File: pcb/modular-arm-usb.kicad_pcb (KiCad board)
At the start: 2 copper layers, 0 parts

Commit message: made a usb-a plug from usb-if and wikipedia docs
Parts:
- added CON1: ARM-SWD-HEADER, pin_array_5x2_50mil_smd, F.Cu at (142.5, 93.0)
- added P1: USB, USB_A_PCB, F.Cu at (115.6, 97.8)
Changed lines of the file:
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@@
 (kicad_pcb (version 3) (host pcbnew "(2013-07-07 BZR 4022)-stable")
   (general
-    (links 0)
-    (no_connects 0)
+    (links 3)
+    (no_connects 3)
     (area 0 0 0 0)
     (thickness 1.6)
@@
     (tracks 0)
     (zones 0)
-    (modules 0)
-    (nets 1)
+    (modules 2)
+    (nets 10)
   )
   (page A3)
@@
     (mod_text_size 1 1)
     (mod_text_width 0.15)
-    (pad_size 1.5 1.5)
-    (pad_drill 0.6)
+    (pad_size 1.143 7.6)
+    (pad_drill 0)
     (pad_to_mask_clearance 0)
     (aux_axis_origin 0 0)
-    (visible_elements FFFFFFBF)
+    (visible_elements 7FFFFFFF)
     (pcbplotparams
       (layerselection 3178497)
@@
   )
   (net 0 "")
+  (net 1 /lpc-mcu/SWCLK)
+  (net 2 /lpc-mcu/SWDIO)
+  (net 3 /lpc-mcu/SWO)
+  (net 4 /lpc-mcu/nRESET)
+  (net 5 /usb/DM)
+  (net 6 /usb/DP)
+  (net 7 GND)
+  (net 8 N-0000011)
+  (net 9 VUSB)
   (net_class Default "This is the default net class."
     (clearance 0.254)
@@
     (uvia_drill 0.127)
     (add_net "")
+    (add_net /lpc-mcu/SWCLK)
+    (add_net /lpc-mcu/SWDIO)
+    (add_net /lpc-mcu/SWO)
+    (add_net /lpc-mcu/nRESET)
+    (add_net /usb/DM)
+    (add_net /usb/DP)
+    (add_net GND)
+    (add_net N-0000011)
+    (add_net VUSB)
+  )
+  (module pin_array_5x2_50mil_smd (layer F.Cu)
+    (at 142.494 92.964)
+    (descr "Double rangee de contacts 2 x 4 pins")
+    (tags CONN)
+    (fp_text reference CON1 (at -4.445 0 90) (layer F.SilkS)
+      (effects (font (size 1.016 1.016) (thickness 0.2032)))
+    )
+    (fp_text value ARM-SWD-HEADER (at 4.318 0 90) (layer F.SilkS) hide
+      (effects (font (size 1.016 1.016) (thickness 0.2032)))
+    )
+    (fp_line (start -1.905 0.381) (end -3.302 0.381) (layer F.SilkS) (width 0.15))
+    (fp_line (start -3.302 0.381) (end -3.302 3.556) (layer F.SilkS) (width 0.15))
+    (fp_line (start -3.302 3.556) (end -1.905 3.556) (layer F.SilkS) (width 0.15))
+    (fp_line (start -2.54 1.524) (end -2.794 1.905) (layer F.SilkS) (width 0.15))
+    (fp_line (start -2.794 1.905) (end -2.413 1.905) (layer F.SilkS) (width 0.15))
+    (fp_line (start -2.413 1.905) (end -2.286 1.905) (layer F.SilkS) (width 0.15))
+    (fp_line (start -2.286 1.905) (end -2.54 1.524) (layer F.SilkS) (width 0.15))
+    (pad 10 smd rect (at 2.54 -1.95) (size 0.76 2.4)
+      (layers F.Cu F.Paste F.Mask)
+      (net 4 /lpc-mcu/nRESET)
+    )
+    (pad 9 smd rect (at 2.54 1.95) (size 0.76 2.4)
+      (layers F.Cu F.Paste F.Mask)
+      (net 7 GND)
+    )
+    (pad 8 smd rect (at 1.27 -1.95) (size 0.76 2.4)
+      (layers F.Cu F.Paste F.Mask)
+    )
+    (pad 7 smd rect (at 1.27 1.95) (size 0.76 2.4)
+      (layers F.Cu F.Paste F.Mask)
+    )
+    (pad 1 smd rect (at -2.54 1.95) (size 0.76 2.4)
+      (layers F.Cu F.Paste F.Mask)
+      (net 8 N-0000011)
+    )
+    (pad 2 smd rect (at -2.54 -1.95) (size 0.76 2.4)
+      (layers F.Cu F.Paste F.Mask)
+      (net 2 /lpc-mcu/SWDIO)
+    )
+    (pad 3 smd rect (at -1.27 1.95) (size 0.76 2.4)
+      (layers F.Cu F.Paste F.Mask)
+      (net 7 GND)
+    )
+    (pad 4 smd rect (at -1.27 -1.95) (size 0.76 2.4)
+      (layers F.Cu F.Paste F.Mask)
+      (net 1 /lpc-mcu/SWCLK)
+    )
+    (pad 5 smd rect (at 0 1.95) (size 0.76 2.4)
+      (layers F.Cu F.Paste F.Mask)
+      (net 7 GND)
+    )
+    (pad 6 smd rect (at 0 -1.95) (size 0.76 2.4)
+      (layers F.Cu F.Paste F.Mask)
+      (net 3 /lpc-mcu/SWO)
+    )
+    (model pin_array/pins_array_3x2.wrl
+      (at (xyz 0 0 0))
+      (scale (xyz 1 1 1))
+      (rotate (xyz 0 0 0))
+    )
+  )
+  (module USB_A_PCB (layer F.Cu)
+    (at 115.57 97.79 270)
+    (fp_text reference P1 (at 0.05 0.75 270) (layer F.SilkS) hide
+      (effects (font (size 1 1) (thickness 0.15)))
+    )
+    (fp_text value USB (at 0.125 -1.1 270) (layer F.SilkS)
+      (effects (font (size 1 1) (thickness 0.15)))
+    )
+    (fp_line (start -6 -8.65) (end -6 -1) (layer F.SilkS) (width 0.15))
+    (fp_line (start 6 -1) (end 6 -8.65) (layer F.SilkS) (width 0.15))
+    (fp_line (start -5 0) (end 5 0) (layer F.SilkS) (width 0.15))
+    (fp_arc (start 5 -1) (end 6 -1) (angle 90) (layer F.SilkS) (width 0.15))
+    (fp_arc (start -5 -1) (end -5 0) (angle 90) (layer F.SilkS) (width 0.15))
+    (fp_line (start -4.85 -8.65) (end -4.85 -1.5) (layer F.SilkS) (width 0.15))
+    (fp_line (start 4.85 -1.5) (end 4.85 -8.65) (layer F.SilkS) (width 0.15))
+    (fp_line (start 6 -8.65) (end -6 -8.65) (layer F.SilkS) (width 0.15))
+    (pad 4 smd rect (at -3.48869 -5.2 270) (size 1.143 7.6)
+      (layers F.Cu F.Paste F.Mask)
+      (net 7 GND)
+    )
+    (pad 3 smd rect (at -0.98679 -5.7 270) (size 1.143 6.6)
+      (layers F.Cu F.Paste F.Mask)
+      (net 6 /usb/DP)
+    )
+    (pad 2 smd rect (at 0.98679 -5.7 270) (size 1.143 6.6)
+      (layers F.Cu F.Paste F.Mask)
+      (net 5 /usb/DM)
+    )
+    (pad 1 smd rect (at 3.48869 -5.2 270) (size 1.143 7.6)
+      (layers F.Cu F.Paste F.Mask)
+      (net 9 VUSB)
+    )
   )
 )

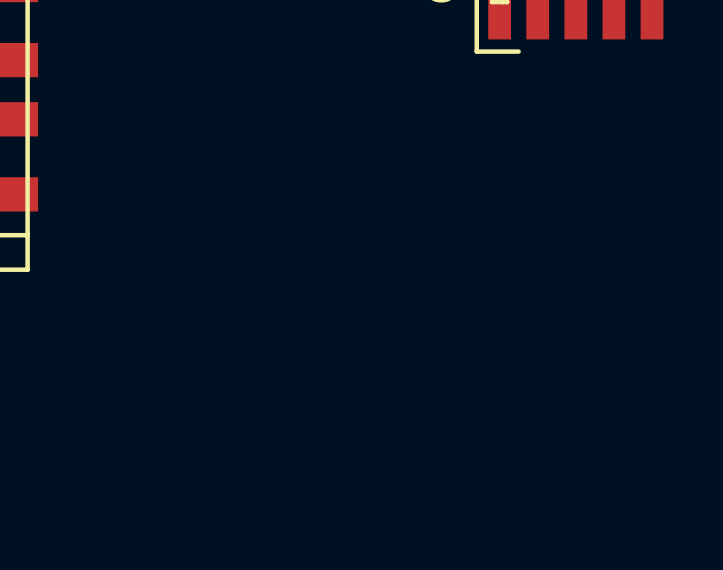
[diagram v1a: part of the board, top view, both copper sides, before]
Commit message: made a footprint for the lpc11u14 that should be nice to hand solder
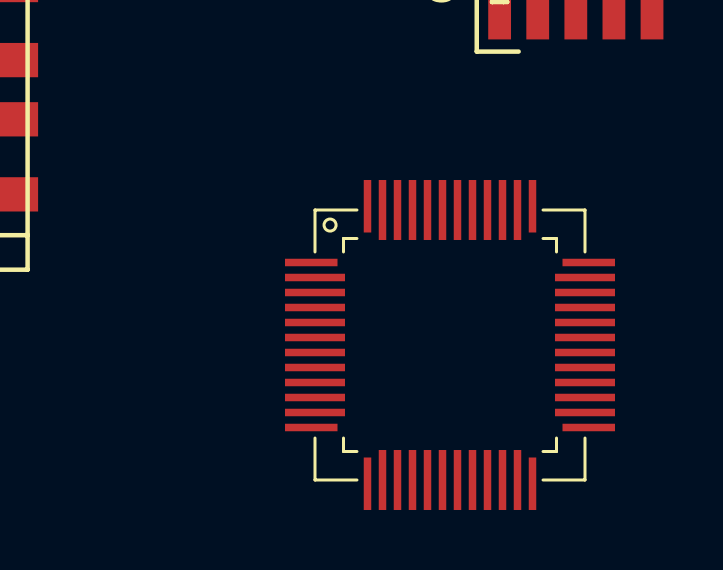
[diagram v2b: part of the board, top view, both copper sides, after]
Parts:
- added IC1: LPC11U14FBD48, NXP_LQFP48_BY_HAND, F.Cu at (138.3, 106.3)
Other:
- net class Default: clearance 0.254 -> 0.1524; trace_width 0.254 -> 0.1524; via_dia 0.889 -> 0.6858; via_drill 0.635 -> 0.3302
- rule trace_clearance: 0.254 -> 0.1524
- rule trace_min: 0.254 -> 0.1524
- rule via_min_drill: 0.508 -> 0.3302
- rule via_min_size: 0.889 -> 0.6858

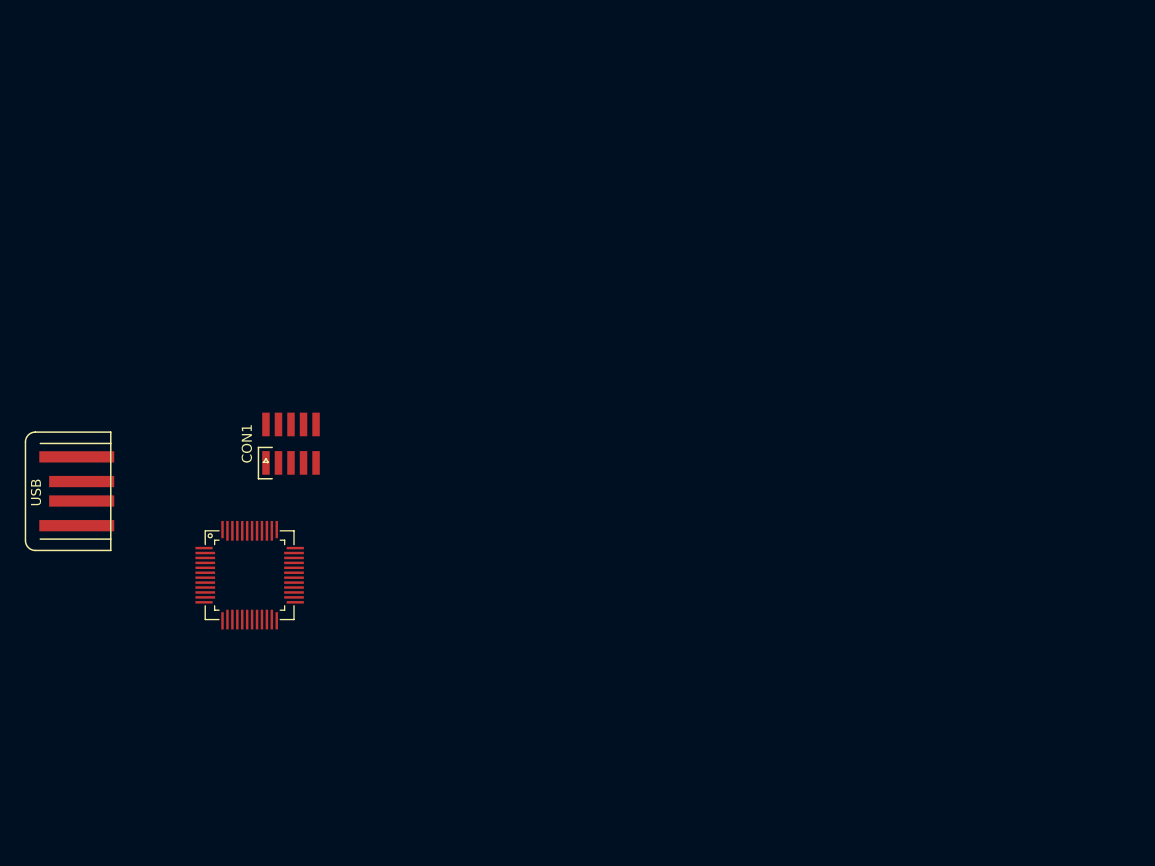
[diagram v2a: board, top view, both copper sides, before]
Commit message: pulled in regulator footprint, started on pcb
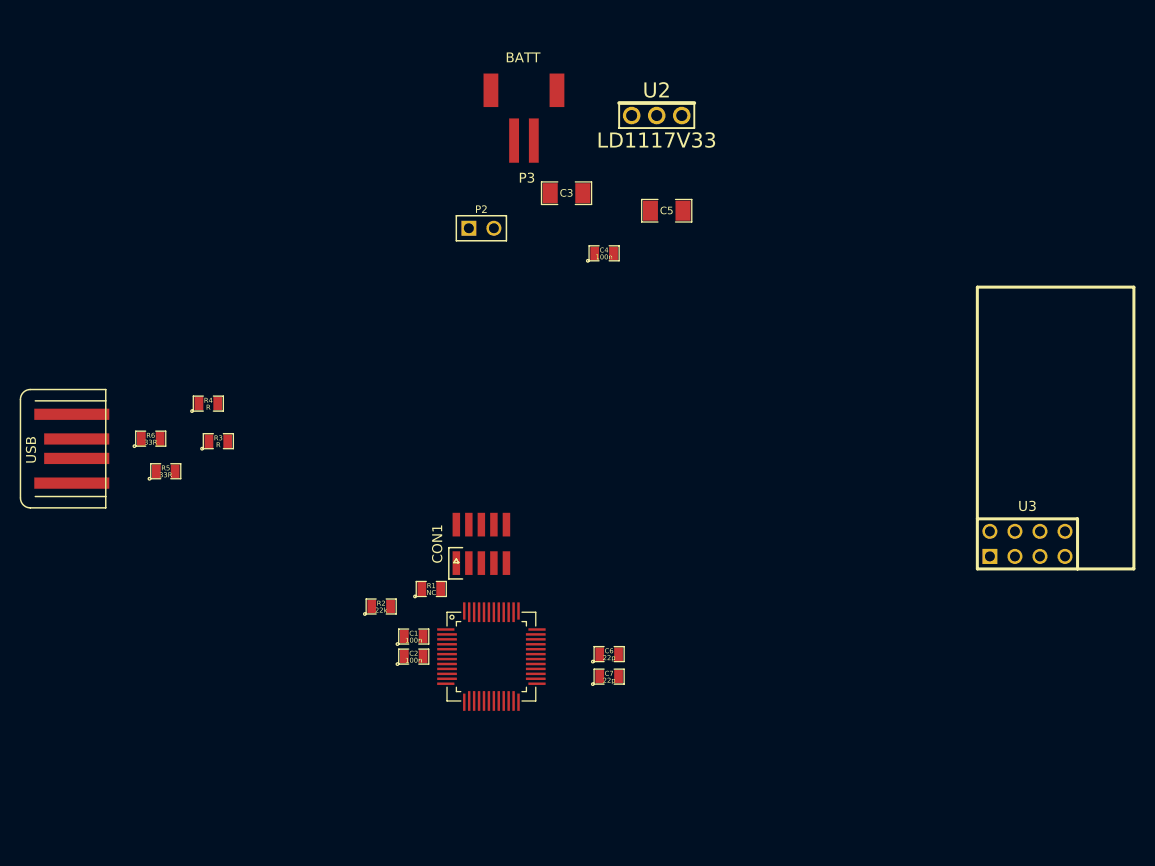
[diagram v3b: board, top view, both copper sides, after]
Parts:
- added C1: 100n, SM0805, F.Cu at (154.9, 112.5)
- added C2: 100n, SM0805, F.Cu at (154.9, 114.6)
- added C3: 22u, SM1206, F.Cu at (170.4, 67.6)
- added C4: 100n, SM0805, F.Cu at (174.2, 73.7)
- added C5: 22u, SM1206, F.Cu at (180.6, 69.3)
- added C6: 22p, SM0805, F.Cu at (174.8, 114.3)
- added C7: 22p, SM0805, F.Cu at (174.8, 116.6)
- added P2: UNFUSED_PWR, PIN_ARRAY_2X1, F.Cu at (161.8, 71.1)
- added P3: BATT, S2B-PH-SM4-TB(LF)(SN), F.Cu at (166.1, 62.2)
- added R1: NC, SM0805, F.Cu at (156.7, 107.7)
- added R2: 22k, SM0805, F.Cu at (151.6, 109.5)
- added R3: R, SM0805, F.Cu at (135.1, 92.7)
- added R4: R, SM0805, F.Cu at (134.1, 88.9)
- added R5: 33R, SM0805, F.Cu at (129.8, 95.8)
- added R6: 33R, SM0805, F.Cu at (128.3, 92.5)
- added U2: LD1117V33, LD1117V33, F.Cu at (177.0, 59.7)
- added U3: NRF24L01+, NRF24L01_MODULE, F.Cu at (217.2, 103.1)
- moved IC1 25.9 mm to (162.8, 114.6)
- moved CON1 21.8 mm to (161.8, 103.1)
- moved P1 4.35 mm to (115.1, 93.5)
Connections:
- IC1 pad 6: (no net) -> N-0000014
- IC1 pad 7: (no net) -> N-0000015

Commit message: power and usb - a bit more progress
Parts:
- added C8: 47p, SM0805, F.Cu at (127.5, 85.1)
- added C9: 47p, SM0805, F.Cu at (127.3, 82.5)
- added P4: GPIO, PIN_ARRAY-6X1, F.Cu at (162.8, 126.7)
- added P5: BATT, PIN_ARRAY_2X1, F.Cu at (158.5, 57.4)
- R3: value R -> 1k5 LS
- R4: value R -> 1k5 FS
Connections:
- C3 pad 1: VLED -> N-0000066
- C4 pad 1: VLED -> N-0000066
- P2 pad 1: VLED -> N-0000066
- P3 pad 2: VLED -> N-0000065
- U2 pad 3: VLED -> N-0000066
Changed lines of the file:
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@@
 (kicad_pcb (version 3) (host pcbnew "(2013-07-07 BZR 4022)-stable")
   (general
-    (links 44)
-    (no_connects 44)
+    (links 49)
+    (no_connects 49)
     (area 0 0 0 0)
     (thickness 1.6)
@@
     (tracks 0)
     (zones 0)
-    (modules 20)
-    (nets 16)
+    (modules 24)
+    (nets 17)
   )
   (page A3)
@@
   (net 9 LPC_USB_DM)
   (net 10 LPC_USB_DP)
-  (net 11 N-0000014)
-  (net 12 N-0000015)
-  (net 13 N-0000018)
-  (net 14 VLED)
-  (net 15 VUSB)
+  (net 11 N-0000019)
+  (net 12 N-0000021)
+  (net 13 N-0000022)
+  (net 14 N-0000065)
+  (net 15 N-0000066)
+  (net 16 VUSB)
   (net_class Default "This is the default net class."
     (clearance 0.1524)
@@
     (add_net LPC_USB_DM)
     (add_net LPC_USB_DP)
-    (add_net N-0000014)
-    (add_net N-0000015)
-    (add_net N-0000018)
-    (add_net VLED)
+    (add_net N-0000019)
+    (add_net N-0000021)
+    (add_net N-0000022)
+    (add_net N-0000065)
+    (add_net N-0000066)
     (add_net VUSB)
   )
@@
     (pad 1 smd rect (at -2.54 1.95) (size 0.76 2.4)
       (layers F.Cu F.Paste F.Mask)
-      (net 13 N-0000018)
+      (net 11 N-0000019)
     )
     (pad 2 smd rect (at -2.54 -1.95) (size 0.76 2.4)
@@
     (pad 1 smd rect (at 3.48869 -5.2 270) (size 1.143 7.6)
       (layers F.Cu F.Paste F.Mask)
-      (net 15 VUSB)
+      (net 16 VUSB)
     )
   )
@@
     (pad 7 smd rect (at -4.5 0.25) (size 2 0.25)
       (layers F.Cu F.Paste F.Mask)
-      (net 12 N-0000015)
+      (net 12 N-0000021)
     )
     (pad 6 smd rect (at -4.5 -0.25) (size 2 0.25)
       (layers F.Cu F.Paste F.Mask)
-      (net 11 N-0000014)
+      (net 13 N-0000022)
     )
     (pad 5 smd rect (at -4.5 -0.75) (size 2 0.25)
@@
     (pad 1 smd rect (at -1.651 0) (size 1.524 2.032)
       (layers F.Cu F.Paste F.Mask)
-      (net 14 VLED)
+      (net 15 N-0000066)
     )
     (pad 2 smd rect (at 1.651 0) (size 1.524 2.032)
@@
     (pad 1 smd rect (at -0.9525 0) (size 0.889 1.397)
       (layers F.Cu F.Paste F.Mask)
-      (net 14 VLED)
+      (net 15 N-0000066)
     )
     (pad 2 smd rect (at 0.9525 0) (size 0.889 1.397)
@@
       (effects (font (size 0.50038 0.50038) (thickness 0.10922)))
     )
-    (fp_text value R (at 0 0.381) (layer F.SilkS)
+    (fp_text value "1k5 FS" (at 0 0.381) (layer F.SilkS)
       (effects (font (size 0.50038 0.50038) (thickness 0.10922)))
     )
@@
       (effects (font (size 0.50038 0.50038) (thickness 0.10922)))
     )
-    (fp_text value R (at 0 0.381) (layer F.SilkS)
+    (fp_text value "1k5 LS" (at 0 0.381) (layer F.SilkS)
       (effects (font (size 0.50038 0.50038) (thickness 0.10922)))
     )
@@
     (pad 2 smd rect (at 0.9525 0) (size 0.889 1.397)
       (layers F.Cu F.Paste F.Mask)
-      (net 12 N-0000015)
+      (net 12 N-0000021)
     )
     (model smd/chip_cms.wrl
@@
     (pad 2 smd rect (at 0.9525 0) (size 0.889 1.397)
       (layers F.Cu F.Paste F.Mask)
-      (net 11 N-0000014)
+      (net 13 N-0000022)
     )
     (model smd/chip_cms.wrl
@@
     (pad 2 smd rect (at 0.9525 0) (size 0.889 1.397)
       (layers F.Cu F.Paste F.Mask)
-      (net 13 N-0000018)
+      (net 11 N-0000019)
     )
     (model smd/chip_cms.wrl
@@
     (pad 2 smd rect (at 1 0) (size 1 4.5)
       (layers F.Cu F.Paste F.Mask)
-      (net 14 VLED)
+      (net 14 N-0000065)
     )
     (pad NC smd rect (at -3.35 -5.1) (size 1.5 3.4)
@@
     (pad 1 thru_hole rect (at -1.27 0) (size 1.524 1.524) (drill 1.016)
       (layers *.Cu *.Mask F.SilkS)
-      (net 14 VLED)
+      (net 15 N-0000066)
     )
     (pad 2 thru_hole circle (at 1.27 0) (size 1.524 1.524) (drill 1.016)
@@
     (pad 3 thru_hole circle (at 5.08 0) (size 1.778 1.778) (drill 1.125)
       (layers *.Cu *.Mask F.SilkS)
-      (net 14 VLED)
-    )
-  )
+      (net 15 N-0000066)
+    )
+  )
+  (module SM0805 (layer F.Cu)
+    (at 127.254 82.55)
+    (attr smd)
+    (fp_text reference C9 (at 0 -0.3175) (layer F.SilkS)
+      (effects (font (size 0.50038 0.50038) (thickness 0.10922)))
+    )
+    (fp_text value 47p (at 0 0.381) (layer F.SilkS)
+      (effects (font (size 0.50038 0.50038) (thickness 0.10922)))
+    )
+    (fp_circle (center -1.651 0.762) (end -1.651 0.635) (layer F.SilkS) (width 0.09906))
+    (fp_line (start -0.508 0.762) (end -1.524 0.762) (layer F.SilkS) (width 0.09906))
+    (fp_line (start -1.524 0.762) (end -1.524 -0.762) (layer F.SilkS) (width 0.09906))
+    (fp_line (start -1.524 -0.762) (end -0.508 -0.762) (layer F.SilkS) (width 0.09906))
+    (fp_line (start 0.508 -0.762) (end 1.524 -0.762) (layer F.SilkS) (width 0.09906))
+    (fp_line (start 1.524 -0.762) (end 1.524 0.762) (layer F.SilkS) (width 0.09906))
+    (fp_line (start 1.524 0.762) (end 0.508 0.762) (layer F.SilkS) (width 0.09906))
+    (pad 1 smd rect (at -0.9525 0) (size 0.889 1.397)
+      (layers F.Cu F.Paste F.Mask)
+      (net 6 /usb/DP)
+    )
+    (pad 2 smd rect (at 0.9525 0) (size 0.889 1.397)
+      (layers F.Cu F.Paste F.Mask)
+      (net 8 GND)
+    )
+    (model smd/chip_cms.wrl
+      (at (xyz 0 0 0))
+      (scale (xyz 0.1 0.1 0.1))
+      (rotate (xyz 0 0 0))
+    )
+  )
+  (module SM0805 (layer F.Cu)
+    (at 127.508 85.09)
+    (attr smd)
+    (fp_text reference C8 (at 0 -0.3175) (layer F.SilkS)
+      (effects (font (size 0.50038 0.50038) (thickness 0.10922)))
+    )
+    (fp_text value 47p (at 0 0.381) (layer F.SilkS)
+      (effects (font (size 0.50038 0.50038) (thickness 0.10922)))
+    )
+    (fp_circle (center -1.651 0.762) (end -1.651 0.635) (layer F.SilkS) (width 0.09906))
+    (fp_line (start -0.508 0.762) (end -1.524 0.762) (layer F.SilkS) (width 0.09906))
+    (fp_line (start -1.524 0.762) (end -1.524 -0.762) (layer F.SilkS) (width 0.09906))
+    (fp_line (start -1.524 -0.762) (end -0.508 -0.762) (layer F.SilkS) (width 0.09906))
+    (fp_line (start 0.508 -0.762) (end 1.524 -0.762) (layer F.SilkS) (width 0.09906))
+    (fp_line (start 1.524 -0.762) (end 1.524 0.762) (layer F.SilkS) (width 0.09906))
+    (fp_line (start 1.524 0.762) (end 0.508 0.762) (layer F.SilkS) (width 0.09906))
+    (pad 1 smd rect (at -0.9525 0) (size 0.889 1.397)
+      (layers F.Cu F.Paste F.Mask)
+      (net 5 /usb/DM)
+    )
+    (pad 2 smd rect (at 0.9525 0) (size 0.889 1.397)
+      (layers F.Cu F.Paste F.Mask)
+      (net 8 GND)
+    )
+    (model smd/chip_cms.wrl
+      (at (xyz 0 0 0))
+      (scale (xyz 0.1 0.1 0.1))
+      (rotate (xyz 0 0 0))
+    )
+  )
+  (module PIN_ARRAY-6X1 (layer F.Cu)
+    (at 162.814 126.746)
+    (descr "Connecteur 6 pins")
+    (tags "CONN DEV")
+    (fp_text reference P4 (at 0 -2.159) (layer F.SilkS)
+      (effects (font (size 1.016 1.016) (thickness 0.2032)))
+    )
+    (fp_text value GPIO (at 0 2.159) (layer F.SilkS) hide
+      (effects (font (size 1.016 0.889) (thickness 0.2032)))
+    )
+    (fp_line (start -7.62 1.27) (end -7.62 -1.27) (layer F.SilkS) (width 0.3048))
+    (fp_line (start -7.62 -1.27) (end 7.62 -1.27) (layer F.SilkS) (width 0.3048))
+    (fp_line (start 7.62 -1.27) (end 7.62 1.27) (layer F.SilkS) (width 0.3048))
+    (fp_line (start 7.62 1.27) (end -7.62 1.27) (layer F.SilkS) (width 0.3048))
+    (fp_line (start -5.08 1.27) (end -5.08 -1.27) (layer F.SilkS) (width 0.3048))
+    (pad 1 thru_hole rect (at -6.35 0) (size 1.524 1.524) (drill 1.016)
+      (layers *.Cu *.Mask F.SilkS)
+    )
+    (pad 2 thru_hole circle (at -3.81 0) (size 1.524 1.524) (drill 1.016)
+      (layers *.Cu *.Mask F.SilkS)
+    )
+    (pad 3 thru_hole circle (at -1.27 0) (size 1.524 1.524) (drill 1.016)
+      (layers *.Cu *.Mask F.SilkS)
+    )
+    (pad 4 thru_hole circle (at 1.27 0) (size 1.524 1.524) (drill 1.016)
+      (layers *.Cu *.Mask F.SilkS)
+    )
+    (pad 5 thru_hole circle (at 3.81 0) (size 1.524 1.524) (drill 1.016)
+      (layers *.Cu *.Mask F.SilkS)
+    )
+    (pad 6 thru_hole circle (at 6.35 0) (size 1.524 1.524) (drill 1.016)
+      (layers *.Cu *.Mask F.SilkS)
+    )
+    (model pin_array/pins_array_6x1.wrl
+      (at (xyz 0 0 0))
+      (scale (xyz 1 1 1))
+      (rotate (xyz 0 0 0))
+    )
+  )
+  (module PIN_ARRAY_2X1 (layer F.Cu)
+    (at 158.496 57.404)
+    (descr "Connecteurs 2 pins")
+    (tags "CONN DEV")
+    (fp_text reference P5 (at 0 -1.905) (layer F.SilkS)
+      (effects (font (size 0.762 0.762) (thickness 0.1524)))
+    )
+    (fp_text value BATT (at 0 -1.905) (layer F.SilkS) hide
+      (effects (font (size 0.762 0.762) (thickness 0.1524)))
+    )
+    (fp_line (start -2.54 1.27) (end -2.54 -1.27) (layer F.SilkS) (width 0.1524))
+    (fp_line (start -2.54 -1.27) (end 2.54 -1.27) (layer F.SilkS) (width 0.1524))
+    (fp_line (start 2.54 -1.27) (end 2.54 1.27) (layer F.SilkS) (width 0.1524))
+    (fp_line (start 2.54 1.27) (end -2.54 1.27) (layer F.SilkS) (width 0.1524))
+    (pad 1 thru_hole rect (at -1.27 0) (size 1.524 1.524) (drill 1.016)
+      (layers *.Cu *.Mask F.SilkS)
+      (net 14 N-0000065)
+    )
+    (pad 2 thru_hole circle (at 1.27 0) (size 1.524 1.524) (drill 1.016)
+      (layers *.Cu *.Mask F.SilkS)
+      (net 8 GND)
+    )
+    (model pin_array/pins_array_2x1.wrl
+      (at (xyz 0 0 0))
+      (scale (xyz 1 1 1))
+      (rotate (xyz 0 0 0))
+    )
+  )
